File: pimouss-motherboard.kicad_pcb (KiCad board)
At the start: 4 copper layers, 281 parts, among them J1 Conn_02x10_Odd_Even, J10 Barrel_Jack_Switch, J2 TMS-105-57-GD, J3 Conn_02x10_Odd_Even, J4 Conn_01x03_Male, J5 Micro_SD_Card_Det, J9 RJSAE-5x8, P1 QSH-060-01-L-D-A, P2 PCIE-064-02, P3 MPCIE-Socket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

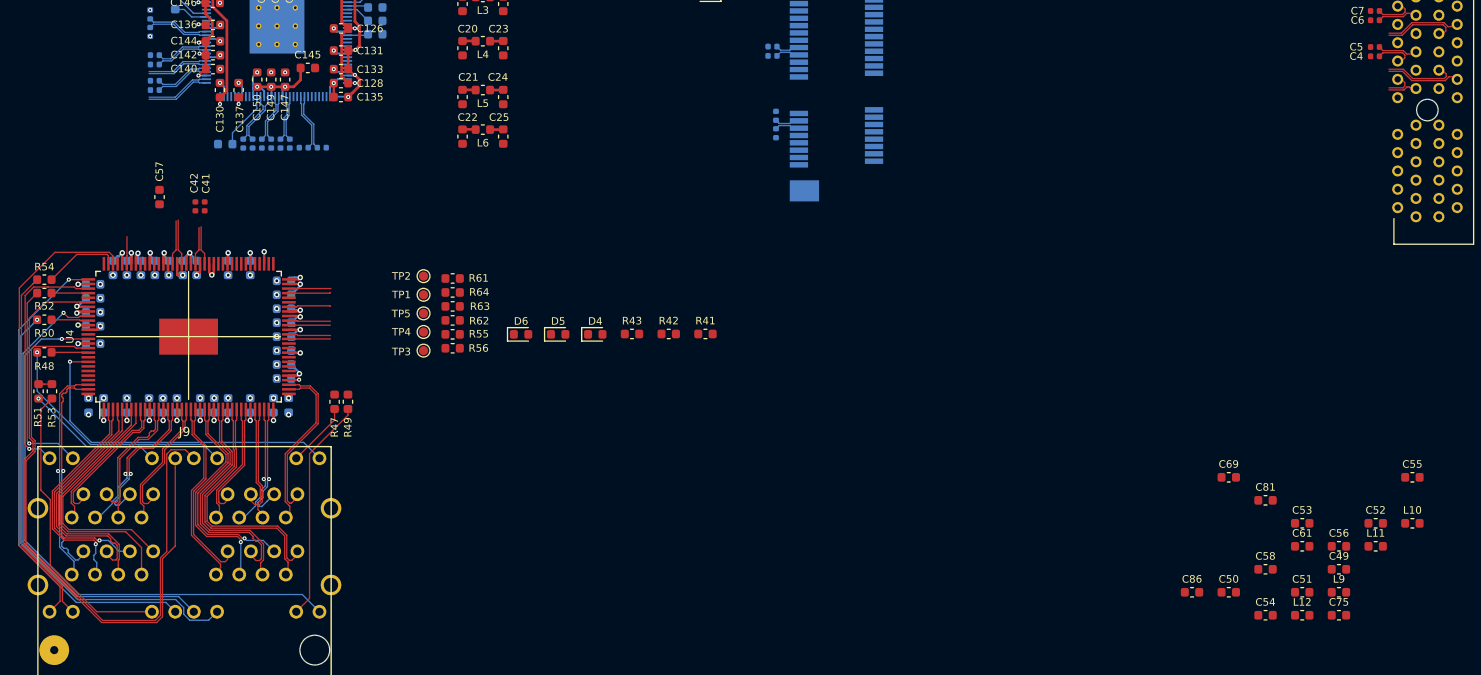
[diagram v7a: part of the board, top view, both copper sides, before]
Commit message: pcb: PHY PSU wiring done
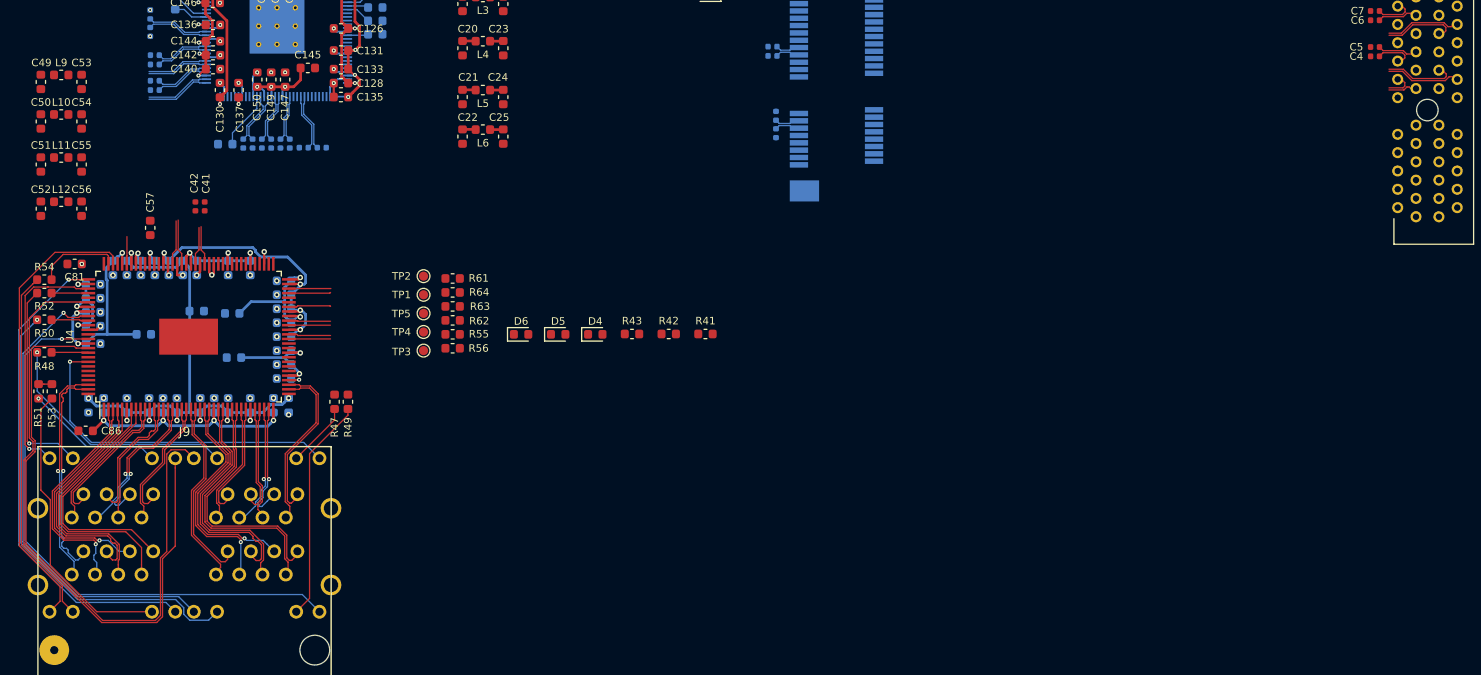
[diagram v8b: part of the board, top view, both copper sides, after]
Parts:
- C58, C61, C69, C75: moved to B.Cu
- moved L10 154.1 mm to (24.7, 99.9)
- moved C49 151.4 mm to (22.5, 96.4), turned to 270 degrees
- moved L9 150.5 mm to (24.7, 95.6)
- moved C52 149.7 mm to (22.5, 110.2), turned to 270 degrees
- moved L11 149.7 mm to (24.7, 104.6)
- moved C55 149.3 mm to (26.9, 105.4), turned to 270 degrees
- moved C51 145.4 mm to (22.5, 105.4), turned to 270 degrees
- moved L12 142.8 mm to (24.7, 109.5)
- moved C56 142.1 mm to (26.9, 110.2), turned to 270 degrees
- moved C53 141.7 mm to (26.9, 96.4), turned to 270 degrees
- moved C54 140.1 mm to (26.9, 100.7), turned to 270 degrees
- moved C50 139.5 mm to (22.5, 100.7), turned to 270 degrees
- moved C81 132.6 mm to (26.2, 116.3), turned to 180 degrees
- moved C61 128.6 mm to (33.7, 124.0)
- moved C75 123.9 mm to (43.6, 126.5), turned to 180 degrees
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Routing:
- net +1V8A: track 24.8 -> 78.6 mm
- net VphyDVDD: track 18.9 -> 59.1 mm, vias 8 -> 9
- net +3V3: track 17.7 -> 46.5 mm
- net +3V3A: track 8.31 -> 30.0 mm
- net VphyVDDC: track 4.95 -> 11.8 mm
- net /phy_data/LED_P0_1: track 8.28 -> 9.15 mm
